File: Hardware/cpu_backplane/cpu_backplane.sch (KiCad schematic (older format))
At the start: 82 parts, among them J1 USB_B_Micro, J2 Conn_02x02_Odd_Even, J3 Conn_01x06, SW1 SW_SPST, U1 74AC161, U2 MAX811SEUS-T, U3 MAX811SEUS-T, U4 PAL24, U5 GAL16V8, U6 W65C02SxP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

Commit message: Fix missing signals
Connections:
- net labels added: ~SIRQ~
- wire segments 221 -> 224
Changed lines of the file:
@@
 Wire Wire Line
 	11600 6200 12000 6200
+Text GLabel 6650 5950 0    50   Input ~ 0
+CLK
+Wire Wire Line
+	6950 5950 6650 5950
+Text GLabel 14050 2000 2    50   Input ~ 0
+~SIRQ~
+Wire Wire Line
+	14050 2000 13850 2000
+Text GLabel 6550 6150 0    50   Output ~ 0
+~SIRQ~
+Wire Wire Line
+	6950 6150 6550 6150
 $EndSCHEMATC

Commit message: Finishing CPU backplane with through hole components
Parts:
- removed H4: MountingHole_Pad, MountingHole:MountingHole_3.2mm_M3_Pad, symbol Mechanical:MountingHole_Pad
- removed R7: 1k, Resistor_SMD:R_0805_2012Metric_Pad1.15x1.40mm_HandSolder, symbol Device:R_Small
- removed X2: SG-7050CAN, Oscillator:Oscillator_SMD_SeikoEpson_SG8002CA-4Pin_7.0x5.0mm, symbol Oscillator:SG-7050CAN
- added C17: 10n, Capacitor_THT:C_Disc_D4.3mm_W1.9mm_P5.00mm, symbol Device:C_Small
- added J4: Conn_01x14, Connector_PinSocket_2.54mm:PinSocket_1x14_P2.54mm_Vertical, symbol Connector_Generic:Conn_01x14
- added R24, R25, R26, R27: 10k, Resistor_THT:R_Axial_DIN0204_L3.6mm_D1.6mm_P5.08mm_Horizontal, symbol Device:R_Small
- added X3: 1.8432MHz, Oscillator:Oscillator_DIP-8, symbol Oscillator:CXO_DIP8
- C1, C10, C11, C12, C14, C15, C16, C2, C3, C4, C5, C6, C7, C8, C9: footprint Capacitor_SMD:C_1206_3216Metric_Pad1.42x1.75mm_HandSolder -> Capacitor_THT:C_Disc_D4.3mm_W1.9mm_P5.00mm
- D1, LED1, LED2, LED3, LED4, LED5, LED6: footprint LED_SMD:LED_1206_3216Metric_Pad1.42x1.75mm_HandSolder -> LED_THT:LED_D3.0mm
- D2, D3, D4, D5, D6, D7, D8: footprint Diode_SMD:D_0805_2012Metric_Pad1.15x1.40mm_HandSolder -> Diode_THT:D_DO-35_SOD27_P7.62mm_Horizontal
- J1: symbol Connector:USB_B_Micro -> cpu_backplane-rescue:USB_B_Micro-Connector
- R1, R10, R11, R12, R13, R14, R15, R16, R17, R18, R19, R2, R20, R21, R22, R23, R3, R4, R5, R6, R8, R9: footprint Resistor_SMD:R_0805_2012Metric_Pad1.15x1.40mm_HandSolder -> Resistor_THT:R_Axial_DIN0204_L3.6mm_D1.6mm_P5.08mm_Horizontal
- U1: footprint Package_SO:SOIC-16_3.9x9.9mm_P1.27mm -> Package_DIP:DIP-16_W7.62mm_Socket
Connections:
- net labels removed: LDE4
- wire segments 224 -> 239
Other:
- moved on the sheet: C14, U4

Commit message: replace resistors with bigger ones + fix diodes
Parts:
- removed LED5, LED6: LED, LED_THT:LED_D3.0mm, symbol Device:LED
- removed R19, R20: 470R, Resistor_THT:R_Axial_DIN0204_L3.6mm_D1.6mm_P5.08mm_Horizontal, symbol Device:R_Small
- C7: value 47n -> 1u
- D2, D3, D4, D5, D6, D7, D8: symbol pspice:DIODE -> Device:D
- R1, R8: value 4.7k -> 10k; footprint Resistor_THT:R_Axial_DIN0204_L3.6mm_D1.6mm_P5.08mm_Horizontal -> Resistor_THT:R_Axial_DIN0207_L6.3mm_D2.5mm_P7.62mm_Horizontal
- R10, R11, R12, R13, R14, R15, R16, R17, R18, R2, R21, R22, R23, R24, R25, R26, R3, R4, R5, R6, R9: footprint Resistor_THT:R_Axial_DIN0204_L3.6mm_D1.6mm_P5.08mm_Horizontal -> Resistor_THT:R_Axial_DIN0207_L6.3mm_D2.5mm_P7.62mm_Horizontal
- U8: footprint Socket:DIP_Socket-28_W11.9_W12.7_W15.24_W17.78_W18.5_3M_228-1277-00-0602J -> Package_DIP:DIP-28_W15.24mm_Socket
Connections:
- net ~ROM_CS~: now also D8.1 (K); no longer D8.2 (A)
- net ~SLOW~: now also D2.2 (A), D3.2 (A), D4.2 (A), D5.2 (A), D6.2 (A), D7.2 (A), D8.2 (A); no longer D2.1 (K), D3.1 (K), D4.1 (K), D5.1 (K), D6.1 (K), D7.1 (K), D8.1 (K)
- net at SLOT2.22 (Pin_22): now also D6.1 (K); no longer D6.2 (A)
- net at SLOT4.22 (Pin_22): now also D2.1 (K); no longer D2.2 (A)
- net at SLOT5.22 (Pin_22): now also D5.1 (K); no longer D5.2 (A)
- net at SLOT1.22 (Pin_22): now also D4.1 (K); no longer D4.2 (A)
- net at SLOT3.22 (Pin_22): now also D7.1 (K); no longer D7.2 (A)
- net at SLOT0.22 (Pin_22): now also D3.1 (K); no longer D3.2 (A)

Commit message: cosmetic fixes to backplane
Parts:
- R27: footprint Resistor_THT:R_Axial_DIN0204_L3.6mm_D1.6mm_P5.08mm_Horizontal -> Resistor_THT:R_Axial_DIN0207_L6.3mm_D2.5mm_P7.62mm_Horizontal
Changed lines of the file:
@@
 F 0 "R27" V 13654 6350 50  0000 C CNN
 F 1 "10k" V 13745 6350 50  0000 C CNN
-F 2 "Resistor_THT:R_Axial_DIN0204_L3.6mm_D1.6mm_P5.08mm_Horizontal" H 13850 6350 50  0001 C CNN
+F 2 "Resistor_THT:R_Axial_DIN0207_L6.3mm_D2.5mm_P7.62mm_Horizontal" H 13850 6350 50  0001 C CNN
 F 3 "~" H 13850 6350 50  0001 C CNN
 	1    13850 6350

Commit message: Update build guide
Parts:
- R10, R11, R12, R13, R9: value 470R -> 330R
- R16: value 4.7k -> 2.2K
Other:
- note removed: "Replace IRQ pull up with SLOW pullup"
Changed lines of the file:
@@
 P 3200 5900
 F 0 "R9" V 3004 5900 50  0000 C CNN
-F 1 "470R" V 3095 5900 50  0000 C CNN
+F 1 "330R" V 3095 5900 50  0000 C CNN
 F 2 "Resistor_THT:R_Axial_DIN0207_L6.3mm_D2.5mm_P7.62mm_Horizontal" H 3200 5900 50  0001 C CNN
 F 3 "~" H 3200 5900 50  0001 C CNN
@@
 P 2250 5450
 F 0 "R10" V 2054 5450 50  0000 C CNN
-F 1 "470R" V 2145 5450 50  0000 C CNN
+F 1 "330R" V 2145 5450 50  0000 C CNN
 F 2 "Resistor_THT:R_Axial_DIN0207_L6.3mm_D2.5mm_P7.62mm_Horizontal" H 2250 5450 50  0001 C CNN
 F 3 "~" H 2250 5450 50  0001 C CNN
@@
 P 2250 5900
 F 0 "R11" V 2054 5900 50  0000 C CNN
-F 1 "470R" V 2145 5900 50  0000 C CNN
+F 1 "330R" V 2145 5900 50  0000 C CNN
 F 2 "Resistor_THT:R_Axial_DIN0207_L6.3mm_D2.5mm_P7.62mm_Horizontal" H 2250 5900 50  0001 C CNN
 F 3 "~" H 2250 5900 50  0001 C CNN
@@
 P 2250 6250
 F 0 "R12" V 2054 6250 50  0000 C CNN
-F 1 "470R" V 2145 6250 50  0000 C CNN
+F 1 "330R" V 2145 6250 50  0000 C CNN
 F 2 "Resistor_THT:R_Axial_DIN0207_L6.3mm_D2.5mm_P7.62mm_Horizontal" H 2250 6250 50  0001 C CNN
 F 3 "~" H 2250 6250 50  0001 C CNN
@@
 P 3200 5450
 F 0 "R13" V 3004 5450 50  0000 C CNN
-F 1 "470R" V 3095 5450 50  0000 C CNN
+F 1 "330R" V 3095 5450 50  0000 C CNN
 F 2 "Resistor_THT:R_Axial_DIN0207_L6.3mm_D2.5mm_P7.62mm_Horizontal" H 3200 5450 50  0001 C CNN
 F 3 "~" H 3200 5450 50  0001 C CNN
@@
 P 9650 1100
 F 0 "R16" V 9454 1100 50  0000 C CNN
-F 1 "4.7k" V 9545 1100 50  0000 C CNN
+F 1 "2.2K" V 9545 1100 50  0000 C CNN
 F 2 "Resistor_THT:R_Axial_DIN0207_L6.3mm_D2.5mm_P7.62mm_Horizontal" H 9650 1100 50  0001 C CNN
 F 3 "~" H 9650 1100 50  0001 C CNN
@@
 Text GLabel 4950 9350 2    50   BiDi ~ 0
 ~IRQ5~
-Text Notes 2800 5600 0    50   ~ 0
-Replace IRQ pull up with SLOW pullup
 $Comp
 L Device:D D7

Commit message: update opl2 board status
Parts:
- C6: value 47n -> 1u
- SLOT0, SLOT1, SLOT2, SLOT3, SLOT4, SLOT5: value Conn_01x40 -> Conn_02x25
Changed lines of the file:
@@
 P 2500 3550
 F 0 "SLOT0" H 2550 4967 50  0000 C CNN
-F 1 "Conn_01x40" H 2550 4876 50  0000 C CNN
+F 1 "Conn_02x25" H 2550 4876 50  0000 C CNN
 F 2 "Connector_PinSocket_2.54mm:PinSocket_2x25_P2.54mm_Vertical" H 2500 3550 50  0001 C CNN
 F 3 "~" H 2500 3550 50  0001 C CNN
@@
 P 6800 3600
 F 0 "SLOT2" H 6850 5017 50  0000 C CNN
-F 1 "Conn_01x40" H 6850 4926 50  0000 C CNN
+F 1 "Conn_02x25" H 6850 4926 50  0000 C CNN
 F 2 "Connector_PinSocket_2.54mm:PinSocket_2x25_P2.54mm_Vertical" H 6800 3600 50  0001 C CNN
 F 3 "~" H 6800 3600 50  0001 C CNN
@@
 P 2450 8200
 F 0 "SLOT4" H 2500 9617 50  0000 C CNN
-F 1 "Conn_01x40" H 2500 9526 50  0000 C CNN
+F 1 "Conn_02x25" H 2500 9526 50  0000 C CNN
 F 2 "Connector_PinSocket_2.54mm:PinSocket_2x25_P2.54mm_Vertical" H 2450 8200 50  0001 C CNN
 F 3 "~" H 2450 8200 50  0001 C CNN
@@
 P 4650 8250
 F 0 "SLOT5" H 4700 9667 50  0000 C CNN
-F 1 "Conn_01x40" H 4700 9576 50  0000 C CNN
+F 1 "Conn_02x25" H 4700 9576 50  0000 C CNN
 F 2 "Connector_PinSocket_2.54mm:PinSocket_2x25_P2.54mm_Vertical" H 4650 8250 50  0001 C CNN
 F 3 "~" H 4650 8250 50  0001 C CNN
@@
 P 4500 3550
 F 0 "SLOT1" H 4550 4967 50  0000 C CNN
-F 1 "Conn_01x40" H 4550 4876 50  0000 C CNN
+F 1 "Conn_02x25" H 4550 4876 50  0000 C CNN
 F 2 "Connector_PinSocket_2.54mm:PinSocket_2x25_P2.54mm_Vertical" H 4500 3550 50  0001 C CNN
 F 3 "~" H 4500 3550 50  0001 C CNN
@@
 P 9250 3600
 F 0 "SLOT3" H 9300 5017 50  0000 C CNN
-F 1 "Conn_01x40" H 9300 4926 50  0000 C CNN
+F 1 "Conn_02x25" H 9300 4926 50  0000 C CNN
 F 2 "Connector_PinSocket_2.54mm:PinSocket_2x25_P2.54mm_Vertical" H 9250 3600 50  0001 C CNN
 F 3 "~" H 9250 3600 50  0001 C CNN
@@
 P 8400 3550
 F 0 "C6" H 8492 3596 50  0000 L CNN
-F 1 "47n" H 8492 3505 50  0000 L CNN
+F 1 "1u" H 8492 3505 50  0000 L CNN
 F 2 "Capacitor_THT:C_Disc_D4.3mm_W1.9mm_P5.00mm" H 8400 3550 50  0001 C CNN
 F 3 "~" H 8400 3550 50  0001 C CNN

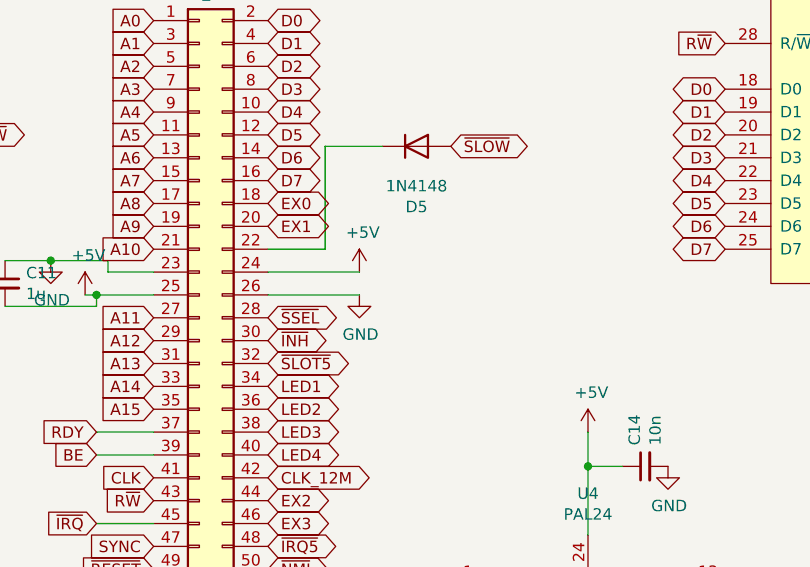
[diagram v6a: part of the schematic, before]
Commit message: add one capacitor for ROM
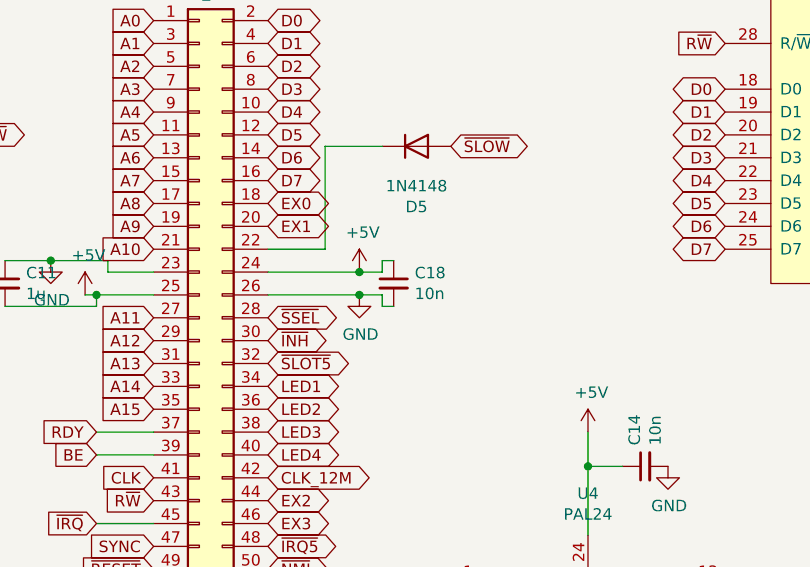
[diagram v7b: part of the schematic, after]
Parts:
- added C18: 10n, Capacitor_THT:C_Disc_D4.3mm_W1.9mm_P5.00mm, symbol Device:C_Small
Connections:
- net +5V: now also C18.1
- net GND: now also C18.2
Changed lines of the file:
@@
 	1    0    0    -1
 $EndComp
+$Comp
+L Device:C_Small C18
+U 1 1 617BF140
+P 5500 8200
+F 0 "C18" H 5592 8246 50  0000 L CNN
+F 1 "10n" H 5592 8155 50  0000 L CNN
+F 2 "Capacitor_THT:C_Disc_D4.3mm_W1.9mm_P5.00mm" H 5500 8200 50  0001 C CNN
+F 3 "~" H 5500 8200 50  0001 C CNN
+	1    5500 8200
+	1    0    0    -1
+$EndComp
+Wire Wire Line
+	5350 8150 5450 8150
+Wire Wire Line
+	5450 8150 5450 8100
+Wire Wire Line
+	5450 8100 5500 8100
+Connection ~ 5350 8150
+Wire Wire Line
+	5500 8300 5450 8300
+Wire Wire Line
+	5450 8300 5450 8250
+Wire Wire Line
+	5450 8250 5350 8250
+Connection ~ 5350 8250
 $EndSCHEMATC

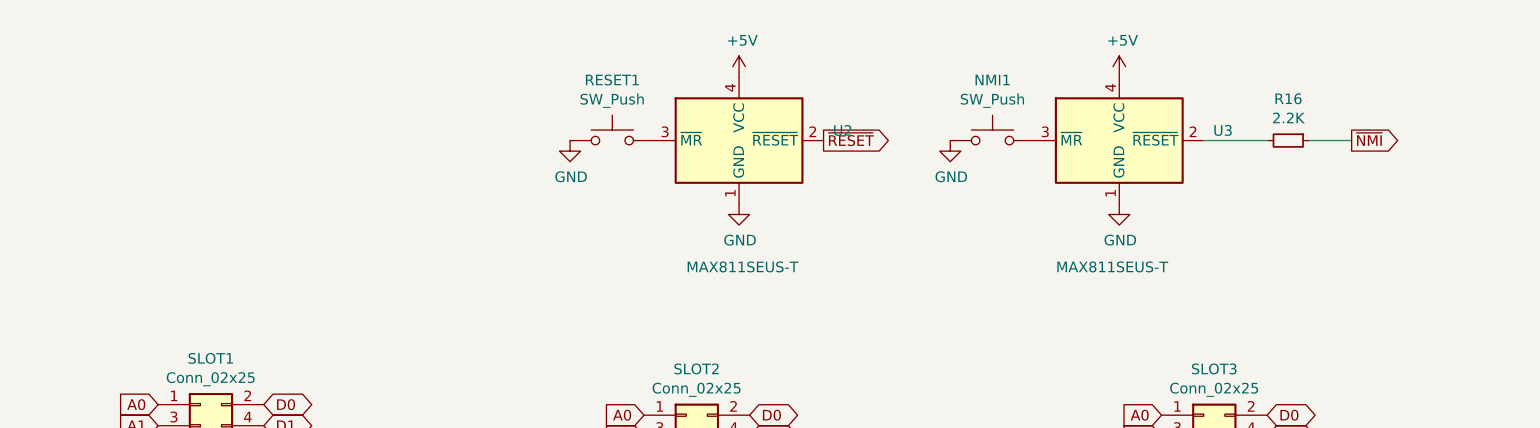
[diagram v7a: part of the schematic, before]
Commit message: update reset and NMI circuits to through hole DS1813
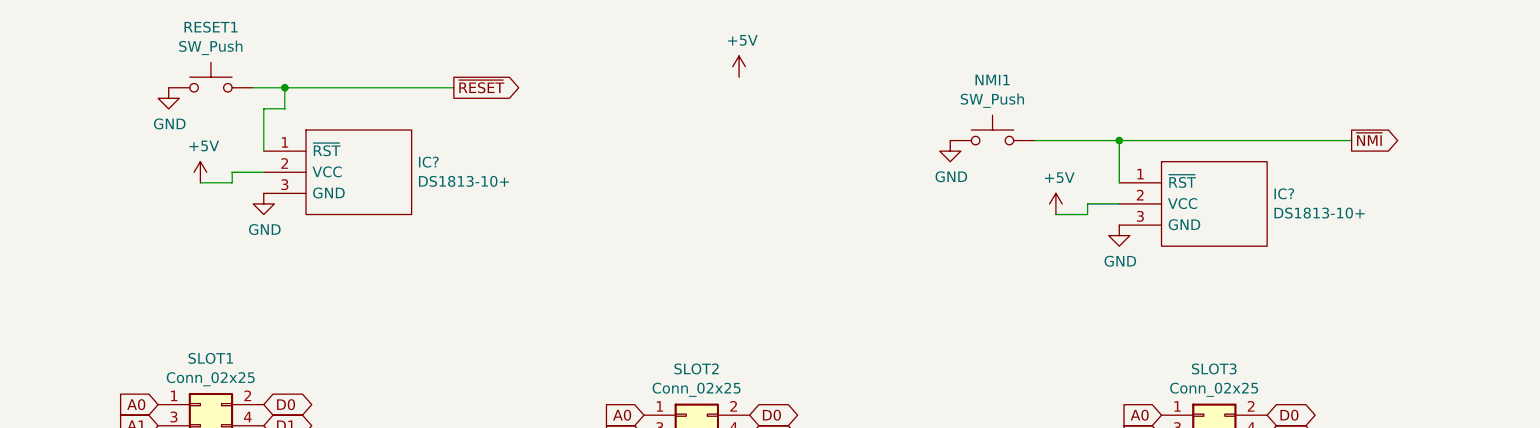
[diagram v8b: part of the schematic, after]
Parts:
- removed R16: 2.2K, Resistor_THT:R_Axial_DIN0207_L6.3mm_D2.5mm_P7.62mm_Horizontal, symbol Device:R_Small
- removed U2, U3: MAX811SEUS-T, Package_TO_SOT_SMD:SOT-143, symbol Power_Supervisor:MAX811SEUS-T
- added IC? (x2): DS1813-10+, Package_TO_SOT_THT:TO-92L_Inline, symbol DS1813-10+:DS1813-10+
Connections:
- net +5V: now also IC?.2 (VCC), IC?.2 (VCC)
- net GND: now also IC?.3 (GND), IC?.3 (GND)
- net ~NMI~: now also NMI1.2, IC?.1 (~RST)
- net ~RESET~: now also RESET1.2, IC?.1 (~RST)
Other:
- moved on the sheet: RESET1
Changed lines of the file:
@@
-	1    0    0    -1
-$EndComp
-$Comp
-L Power_Supervisor:MAX811SEUS-T U3
-U 1 1 600754D0
-P 8850 1100
-F 0 "U3" H 9294 1146 50  0000 L CNN
-F 1 "MAX811SEUS-T" H 8550 500 50  0000 L CNN
-F 2 "Package_TO_SOT_SMD:SOT-143" H 8950 800 50  0001 L CNN
-F 3 "https://datasheets.maximintegrated.com/en/ds/MAX811-MAX812.pdf" H 8500 400 50  0001 C CNN
-	1    8850 1100
-	1    0    0    -1
-$EndComp
-$Comp
-L Power_Supervisor:MAX811SEUS-T U2
-U 1 1 6007822A
-P 7050 1100
-F 0 "U2" H 7494 1146 50  0000 L CNN
-F 1 "MAX811SEUS-T" H 6800 500 50  0000 L CNN
-F 2 "Package_TO_SOT_SMD:SOT-143" H 7150 800 50  0001 L CNN
-F 3 "https://datasheets.maximintegrated.com/en/ds/MAX811-MAX812.pdf" H 6700 400 50  0001 C CNN
-	1    7050 1100
 	1    0    0    -1
 $EndComp
 Text GLabel 9950 1100 2    50   Output ~ 0
 ~NMI~
-Text GLabel 7450 1100 2    50   Output ~ 0
+Text GLabel 5700 850  2    50   Output ~ 0
 ~RESET~
 $Comp
 L power:GND #PWR0135
 U 1 1 6008D891
-P 8850 1400
-F 0 "#PWR0135" H 8850 1150 50  0001 C CNN
-F 1 "GND" H 8855 1227 50  0000 C CNN
-F 2 "" H 8850 1400 50  0001 C CNN
-F 3 "" H 8850 1400 50  0001 C CNN
-	1    8850 1400
-	1    0    0    -1
-$EndComp
-$Comp
-L power:GND #PWR0136
-U 1 1 60092C1C
-P 7050 1400
-F 0 "#PWR0136" H 7050 1150 50  0001 C CNN
-F 1 "GND" H 7055 1227 50  0000 C CNN
-F 2 "" H 7050 1400 50  0001 C CNN
-F 3 "" H 7050 1400 50  0001 C CNN
-	1    7050 1400
+P 8850 1500
+F 0 "#PWR0135" H 8850 1250 50  0001 C CNN
+F 1 "GND" H 8855 1327 50  0000 C CNN
+F 2 "" H 8850 1500 50  0001 C CNN
+F 3 "" H 8850 1500 50  0001 C CNN
+	1    8850 1500
 	1    0    0    -1
 $EndComp
@@
 L power:+5V #PWR0137
 U 1 1 60098175
-P 8850 800
-F 0 "#PWR0137" H 8850 650 50  0001 C CNN
-F 1 "+5V" H 8865 973 50  0000 C CNN
-F 2 "" H 8850 800 50  0001 C CNN
-F 3 "" H 8850 800 50  0001 C CNN
-	1    8850 800
+P 8550 1450
+F 0 "#PWR0137" H 8550 1300 50  0001 C CNN
+F 1 "+5V" H 8565 1623 50  0000 C CNN
+F 2 "" H 8550 1450 50  0001 C CNN
+F 3 "" H 8550 1450 50  0001 C CNN
+	1    8550 1450
 	1    0    0    -1
 $EndComp
@@
 L Switch:SW_Push RESET1
 U 1 1 600A3302
-P 6450 1100
-F 0 "RESET1" H 6450 1385 50  0000 C CNN
-F 1 "SW_Push" H 6450 1294 50  0000 C CNN
-F 2 "Button_Switch_THT:SW_PUSH_6mm" H 6450 1300 50  0001 C CNN
-F 3 "~" H 6450 1300 50  0001 C CNN
-	1    6450 1100
+P 4550 850
+F 0 "RESET1" H 4550 1135 50  0000 C CNN
+F 1 "SW_Push" H 4550 1044 50  0000 C CNN
+F 2 "Button_Switch_THT:SW_PUSH_6mm" H 4550 1050 50  0001 C CNN
+F 3 "~" H 4550 1050 50  0001 C CNN
+	1    4550 850
 	1    0    0    -1
 $EndComp
@@
 L power:GND #PWR0139
 U 1 1 600A3D95
-P 6250 1100
-F 0 "#PWR0139" H 6250 850 50  0001 C CNN
-F 1 "GND" H 6255 927 50  0000 C CNN
-F 2 "" H 6250 1100 50  0001 C CNN
-F 3 "" H 6250 1100 50  0001 C CNN
-	1    6250 1100
+P 4350 850
+F 0 "#PWR0139" H 4350 600 50  0001 C CNN
+F 1 "GND" H 4355 677 50  0000 C CNN
+F 2 "" H 4350 850 50  0001 C CNN
+F 3 "" H 4350 850 50  0001 C CNN
+	1    4350 850
 	1    0    0    -1
 $EndComp
@@
 Wire Wire Line
 	1200 1050 1700 1050
-Wire Wire Line
-	9950 1100 9750 1100
-Wire Wire Line
-	9550 1100 9250 1100
-$Comp
-L Device:R_Small R16
-U 1 1 60052F9C
-P 9650 1100
-F 0 "R16" V 9454 1100 50  0000 C CNN
-F 1 "2.2K" V 9545 1100 50  0000 C CNN
-F 2 "Resistor_THT:R_Axial_DIN0207_L6.3mm_D2.5mm_P7.62mm_Horizontal" H 9650 1100 50  0001 C CNN
-F 3 "~" H 9650 1100 50  0001 C CNN
-	1    9650 1100
-	0    1    1    0
-$EndComp
 Text GLabel 5750 9500 0    50   Input ~ 0
 CLK
@@
 	5450 8250 5350 8250
 Connection ~ 5350 8250
+$Comp
+L DS1813-10+:DS1813-10+ IC?
+U 1 1 618021F5
+P 8850 1300
+F 0 "IC?" H 9578 1246 50  0000 L CNN
+F 1 "DS1813-10+" H 9578 1155 50  0000 L CNN
+F 2 "Package_TO_SOT_THT:TO-92L_Inline" H 9600 1400 50  0001 L CNN
+F 3 "" H 9600 1300 50  0001 L CNN
+F 4 "TO92 uP supervisor chip,DS1813-10 4.35V" H 9600 1200 50  0001 L CNN "Description"
+F 5 "5" H 9600 1100 50  0001 L CNN "Height"
+F 6 "" H 9600 1000 50  0001 L CNN "Mouser Part Number"
+F 7 "" H 9600 900 50  0001 L CNN "Mouser Price/Stock"
+F 8 "Maxim Integrated" H 9600 800 50  0001 L CNN "Manufacturer_Name"
+F 9 "DS1813-10+" H 9600 700 50  0001 L CNN "Manufacturer_Part_Number"
+	1    8850 1300
+	1    0    0    -1
+$EndComp
+Wire Wire Line
+	8850 1400 8700 1400
+Wire Wire Line
+	8700 1400 8700 1450
+Wire Wire Line
+	8700 1450 8550 1450
+Wire Wire Line
+	8450 1100 8850 1100
+Wire Wire Line
+	8850 1300 8850 1100
+Connection ~ 8850 1100
+Wire Wire Line
+	8850 1100 9950 1100
+$Comp
+L power:GND #PWR?
+U 1 1 618B82E0
+P 4800 1350
+F 0 "#PWR?" H 4800 1100 50  0001 C CNN
+F 1 "GND" H 4805 1177 50  0000 C CNN
+F 2 "" H 4800 1350 50  0001 C CNN
+F 3 "" H 4800 1350 50  0001 C CNN
+	1    4800 1350
+	1    0    0    -1
+$EndComp
+$Comp
+L power:+5V #PWR?
+U 1 1 618B82E6
+P 4500 1300
+F 0 "#PWR?" H 4500 1150 50  0001 C CNN
+F 1 "+5V" H 4515 1473 50  0000 C CNN
+F 2 "" H 4500 1300 50  0001 C CNN
+F 3 "" H 4500 1300 50  0001 C CNN
+	1    4500 1300
+	1    0    0    -1
+$EndComp
+$Comp
+L DS1813-10+:DS1813-10+ IC?
+U 1 1 618B82F2
+P 4800 1150
+F 0 "IC?" H 5528 1096 50  0000 L CNN
+F 1 "DS1813-10+" H 5528 1005 50  0000 L CNN
+F 2 "Package_TO_SOT_THT:TO-92L_Inline" H 5550 1250 50  0001 L CNN
+F 3 "" H 5550 1150 50  0001 L CNN
+F 4 "TO92 uP supervisor chip,DS1813-10 4.35V" H 5550 1050 50  0001 L CNN "Description"
+F 5 "5" H 5550 950 50  0001 L CNN "Height"
+F 6 "" H 5550 850 50  0001 L CNN "Mouser Part Number"
+F 7 "" H 5550 750 50  0001 L CNN "Mouser Price/Stock"
+F 8 "Maxim Integrated" H 5550 650 50  0001 L CNN "Manufacturer_Name"
+F 9 "DS1813-10+" H 5550 550 50  0001 L CNN "Manufacturer_Part_Number"
+	1    4800 1150
+	1    0    0    -1
+$EndComp
+Wire Wire Line
+	4800 1250 4650 1250
+Wire Wire Line
+	4650 1250 4650 1300
+Wire Wire Line
+	4650 1300 4500 1300
+Wire Wire Line
+	5700 850  4900 850
+Wire Wire Line
+	4800 1150 4800 950
+Wire Wire Line
+	4800 950  4900 950
+Wire Wire Line
+	4900 950  4900 850
+Connection ~ 4900 850
+Wire Wire Line
+	4900 850  4750 850
 $EndSCHEMATC
